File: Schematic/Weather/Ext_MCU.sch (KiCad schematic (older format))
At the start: 3 parts, among them J1 4_Way_Wire, U3 AMS1117, U4 ESP-01v090

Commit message: more changes
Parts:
- added J5, J6: 4_Way_Wire, Connector_PinHeader_2.54mm:PinHeader_1x04_P2.54mm_Vertical, symbol MyComponents:4_Way_Wire
- renumbered J1 to J4, U3 to U2, U4 to U3
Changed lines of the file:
@@
 $Descr A4 11693 8268
 encoding utf-8
-Sheet 6 14
+Sheet 6 15
 Title ""
 Date ""
@@
 P 5550 3650
 AR Path="/5C950A1B" Ref="U?"  Part="1"
-AR Path="/5C93D4CF/5C950A1B" Ref="U4"  Part="1"
-F 0 "U4" H 5550 4165 50  0000 C CNN
+AR Path="/5C93D4CF/5C950A1B" Ref="U3"  Part="1"
+F 0 "U3" H 5550 4165 50  0000 C CNN
 F 1 "ESP-01v090" H 5550 4074 50  0000 C CNN
 F 2 "footprint:ESP-01" H 5550 3650 50  0001 C CNN
@@
 $EndComp
 $Comp
-L MyComponents:4_Way_Wire J1
+L MyComponents:4_Way_Wire J4
 U 1 1 5C964519
 P 3100 3100
-F 0 "J1" H 3050 2350 50  0000 L CNN
+F 0 "J4" H 3050 2350 50  0000 L CNN
 F 1 "4_Way_Wire" H 2850 2200 50  0000 L CNN
 F 2 "Connector_PinHeader_2.54mm:PinHeader_1x04_P2.54mm_Vertical" H 3000 3150 50  0001 C CNN
@@
 $EndComp
 $Comp
-L MyComponents:AMS1117 U3
+L MyComponents:AMS1117 U2
 U 1 1 5C951D08
 P 3200 1950
-F 0 "U3" V 2700 2000 60  0000 R CNN
+F 0 "U2" V 2700 2000 60  0000 R CNN
 F 1 "AMS1117" V 2600 2200 60  0000 R CNN
 F 2 "Package_TO_SOT_SMD:SOT-223-3_TabPin2" H 3200 1950 60  0001 C CNN
@@
 Wire Wire Line
 	4300 3800 4600 3800
+$Comp
+L MyComponents:4_Way_Wire J5
+U 1 1 5CB477D0
+P 3150 4400
+F 0 "J5" H 3319 4161 50  0000 L CNN
+F 1 "4_Way_Wire" H 3319 4070 50  0000 L CNN
+F 2 "Connector_PinHeader_2.54mm:PinHeader_1x04_P2.54mm_Vertical" H 3050 4450 50  0001 C CNN
+F 3 "" H 3050 4450 50  0001 C CNN
+	1    3150 4400
+	1    0    0    -1
+$EndComp
+$Comp
+L MyComponents:4_Way_Wire J6
+U 1 1 5CB50010
+P 3150 5400
+F 0 "J6" H 3319 5161 50  0000 L CNN
+F 1 "4_Way_Wire" H 3319 5070 50  0000 L CNN
+F 2 "Connector_PinHeader_2.54mm:PinHeader_1x04_P2.54mm_Vertical" H 3050 5450 50  0001 C CNN
+F 3 "" H 3050 5450 50  0001 C CNN
+	1    3150 5400
+	1    0    0    -1
+$EndComp
 $EndSCHEMATC

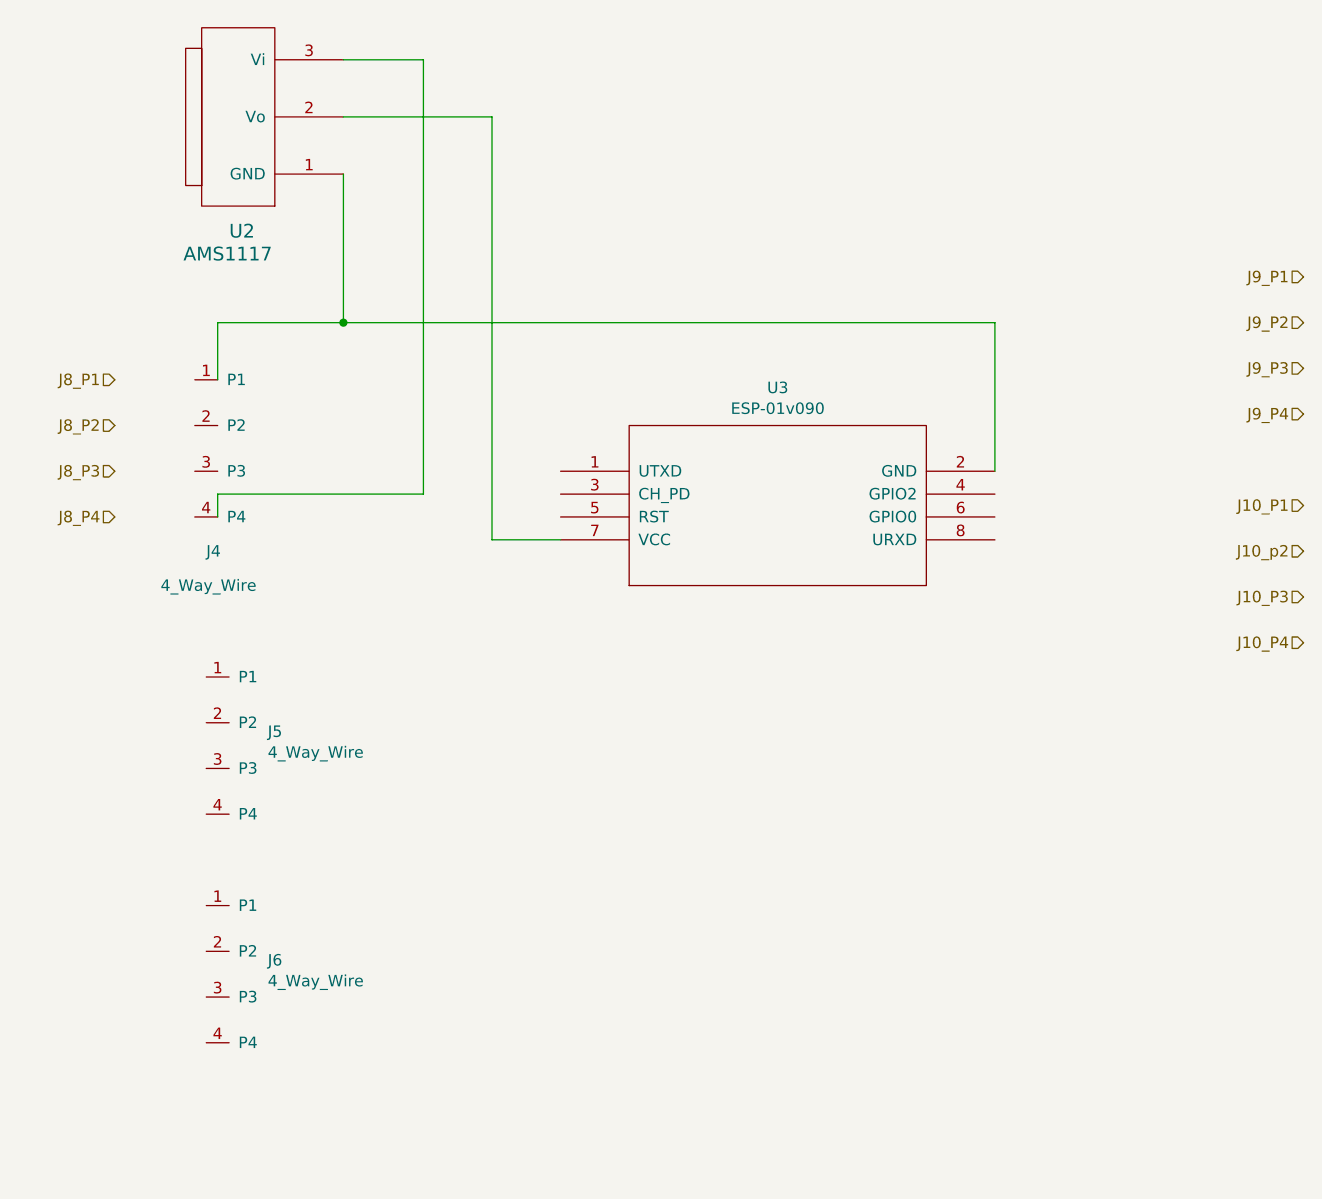
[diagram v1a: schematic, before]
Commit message: Connector relable start
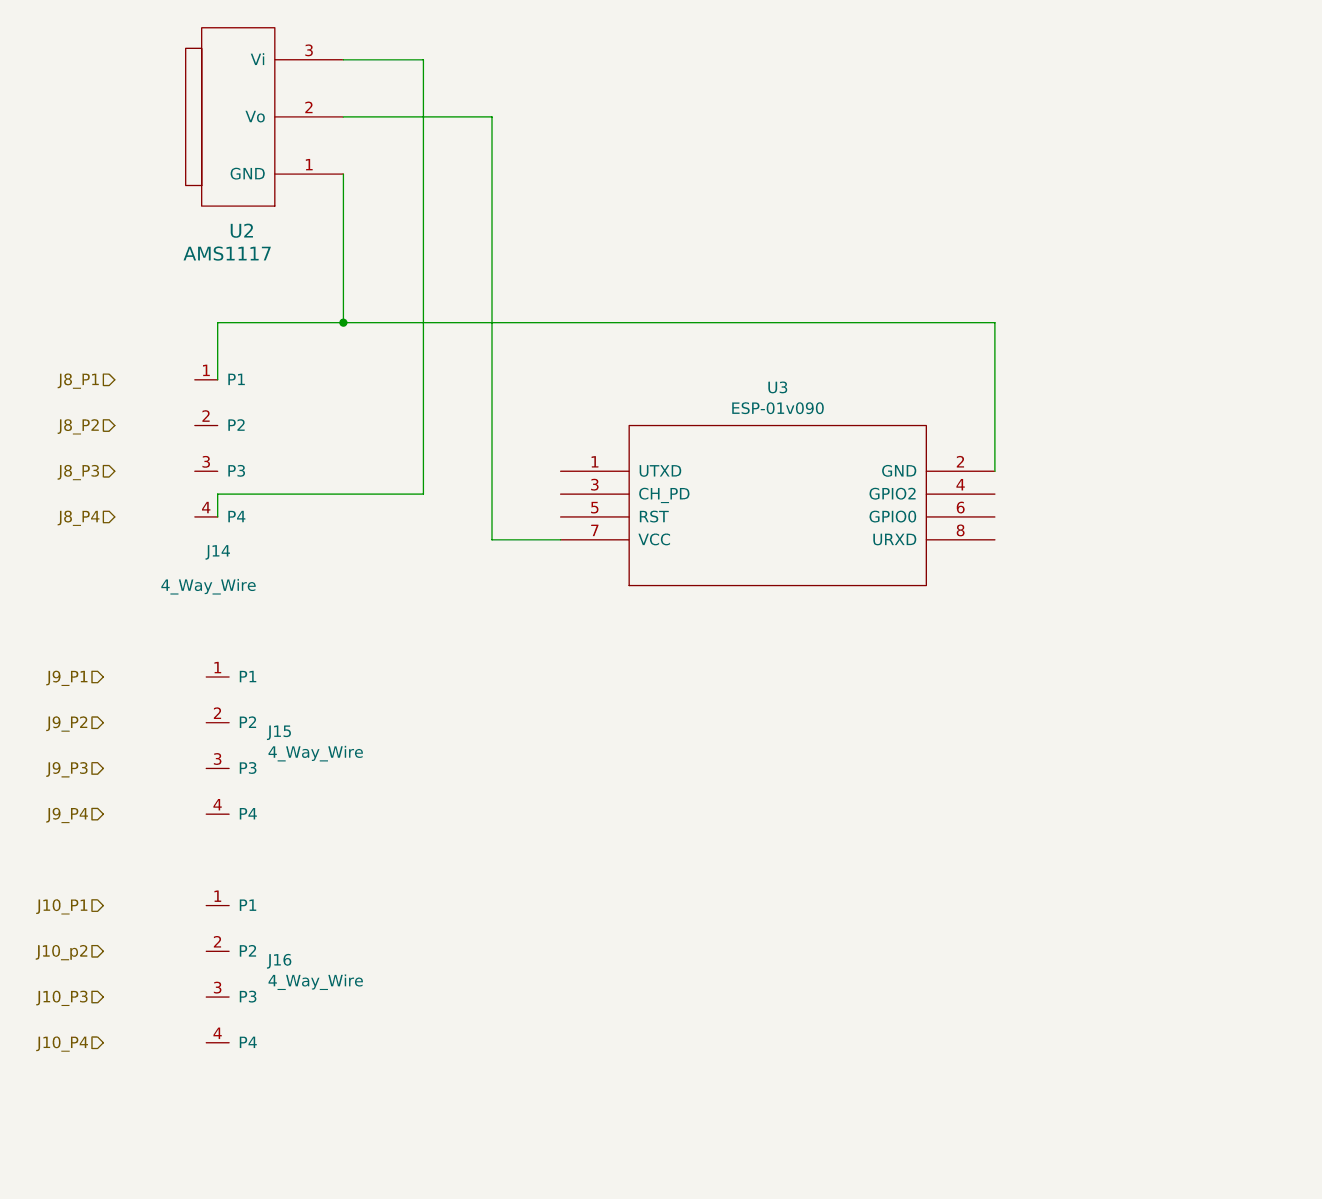
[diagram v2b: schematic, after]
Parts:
- renumbered J4 to J14, J5 to J15, J6 to J16
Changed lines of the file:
@@
 Text HLabel 2650 3700 0    50   Input ~ 0
 J8_P4
-Text HLabel 7850 2650 0    50   Input ~ 0
+Text HLabel 2600 4400 0    50   Input ~ 0
 J9_P1
-Text HLabel 7850 2850 0    50   Input ~ 0
+Text HLabel 2600 4600 0    50   Input ~ 0
 J9_P2
-Text HLabel 7850 3050 0    50   Input ~ 0
+Text HLabel 2600 4800 0    50   Input ~ 0
 J9_P3
-Text HLabel 7850 3250 0    50   Input ~ 0
+Text HLabel 2600 5000 0    50   Input ~ 0
 J9_P4
-Text HLabel 7850 3650 0    50   Input ~ 0
+Text HLabel 2600 5400 0    50   Input ~ 0
 J10_P1
-Text HLabel 7850 3850 0    50   Input ~ 0
+Text HLabel 2600 5600 0    50   Input ~ 0
 J10_p2
-Text HLabel 7850 4050 0    50   Input ~ 0
+Text HLabel 2600 5800 0    50   Input ~ 0
 J10_P3
-Text HLabel 7850 4250 0    50   Input ~ 0
+Text HLabel 2600 6000 0    50   Input ~ 0
 J10_P4
 $Comp
@@
 $EndComp
 $Comp
-L MyComponents:4_Way_Wire J4
+L MyComponents:4_Way_Wire J14
 U 1 1 5C964519
 P 3100 3100
-F 0 "J4" H 3050 2350 50  0000 L CNN
+F 0 "J14" H 3050 2350 50  0000 L CNN
 F 1 "4_Way_Wire" H 2850 2200 50  0000 L CNN
 F 2 "Connector_PinHeader_2.54mm:PinHeader_1x04_P2.54mm_Vertical" H 3000 3150 50  0001 C CNN
@@
 	4300 3800 4600 3800
 $Comp
-L MyComponents:4_Way_Wire J5
+L MyComponents:4_Way_Wire J15
 U 1 1 5CB477D0
 P 3150 4400
-F 0 "J5" H 3319 4161 50  0000 L CNN
+F 0 "J15" H 3319 4161 50  0000 L CNN
 F 1 "4_Way_Wire" H 3319 4070 50  0000 L CNN
 F 2 "Connector_PinHeader_2.54mm:PinHeader_1x04_P2.54mm_Vertical" H 3050 4450 50  0001 C CNN
@@
 $EndComp
 $Comp
-L MyComponents:4_Way_Wire J6
+L MyComponents:4_Way_Wire J16
 U 1 1 5CB50010
 P 3150 5400
-F 0 "J6" H 3319 5161 50  0000 L CNN
+F 0 "J16" H 3319 5161 50  0000 L CNN
 F 1 "4_Way_Wire" H 3319 5070 50  0000 L CNN
 F 2 "Connector_PinHeader_2.54mm:PinHeader_1x04_P2.54mm_Vertical" H 3050 5450 50  0001 C CNN

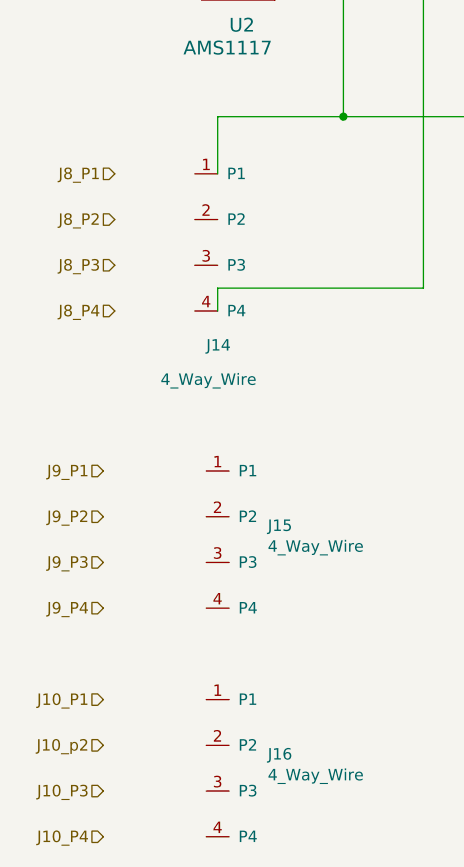
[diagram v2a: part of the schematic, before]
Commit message: Connector changes
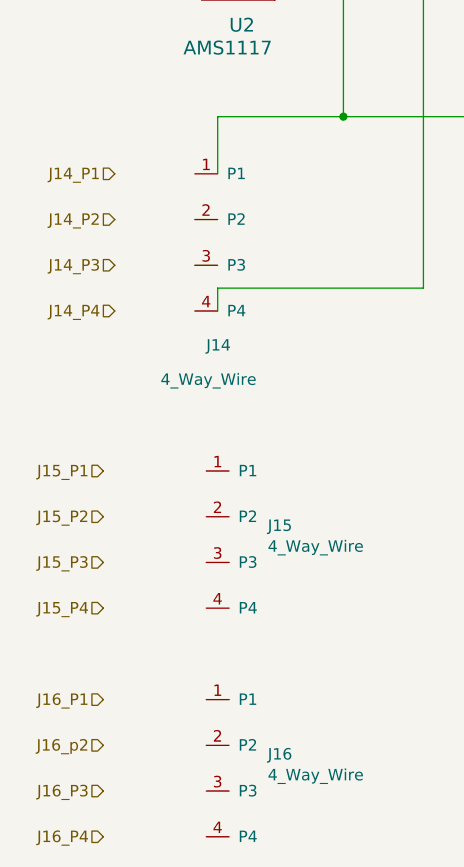
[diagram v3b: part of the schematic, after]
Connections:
- net labels added: J14_P1, J14_P2, J14_P3, J14_P4, J15_P1, J15_P2, J15_P3, J15_P4, J16_P1, J16_P3, J16_P4, J16_p2
- net labels removed: J10_P1, J10_P3, J10_P4, J10_p2, J8_P1, J8_P2, J8_P3, J8_P4, J9_P1, J9_P2, J9_P3, J9_P4
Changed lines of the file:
@@
 $EndDescr
 Text HLabel 2650 3100 0    50   Input ~ 0
-J8_P1
+J14_P1
 Text HLabel 2650 3300 0    50   Input ~ 0
-J8_P2
+J14_P2
 Text HLabel 2650 3500 0    50   Input ~ 0
-J8_P3
+J14_P3
 Text HLabel 2650 3700 0    50   Input ~ 0
-J8_P4
+J14_P4
 Text HLabel 2600 4400 0    50   Input ~ 0
-J9_P1
+J15_P1
 Text HLabel 2600 4600 0    50   Input ~ 0
-J9_P2
+J15_P2
 Text HLabel 2600 4800 0    50   Input ~ 0
-J9_P3
+J15_P3
 Text HLabel 2600 5000 0    50   Input ~ 0
-J9_P4
+J15_P4
 Text HLabel 2600 5400 0    50   Input ~ 0
-J10_P1
+J16_P1
 Text HLabel 2600 5600 0    50   Input ~ 0
-J10_p2
+J16_p2
 Text HLabel 2600 5800 0    50   Input ~ 0
-J10_P3
+J16_P3
 Text HLabel 2600 6000 0    50   Input ~ 0
-J10_P4
+J16_P4
 $Comp
 L Weather-rescue:ESP-01v090-ESP8266 U?
